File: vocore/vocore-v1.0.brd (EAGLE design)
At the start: 25.6 x 25.6 mm, 146 parts, among them CON2 5020, U1 TFBGA196, U25 U4, U3 SO8, U33 Y1, U35 TSOP2-54P-400MIL, U8 LDO1, U9 LDO1

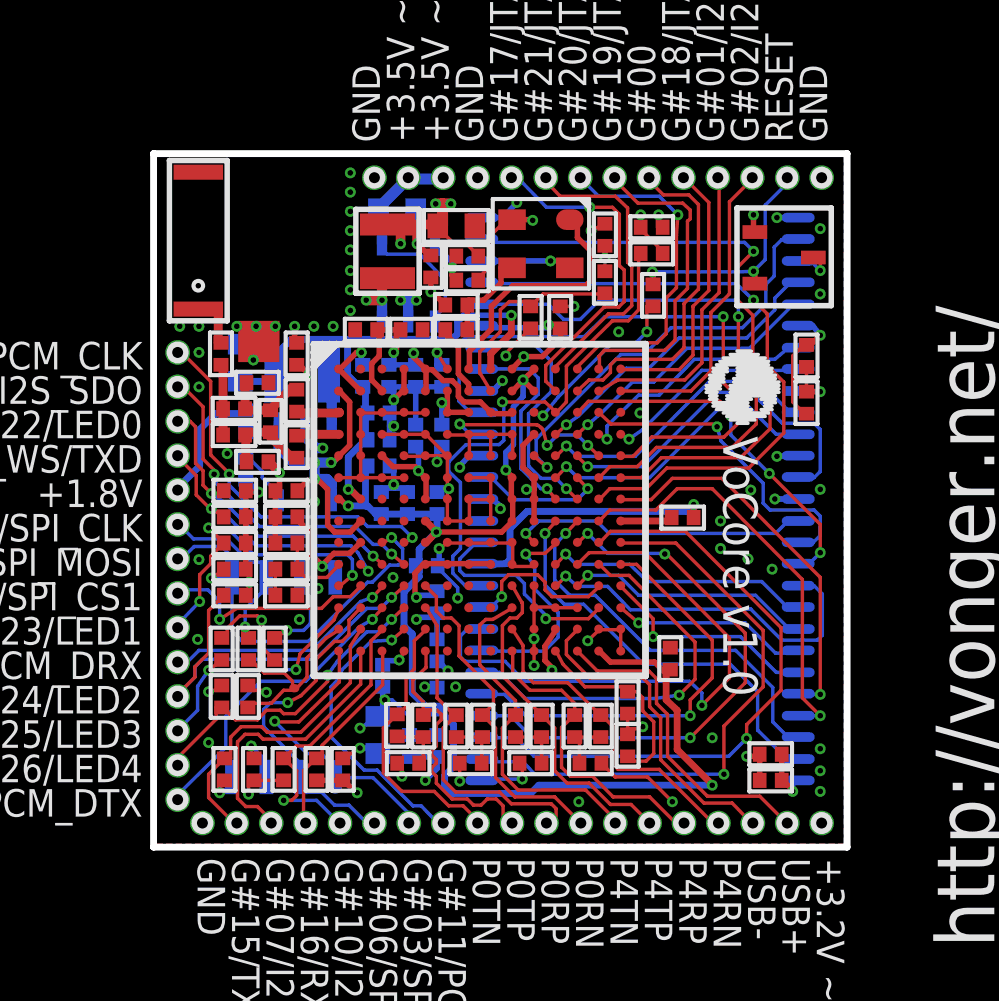
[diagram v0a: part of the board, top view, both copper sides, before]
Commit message: added 4 layer rules.
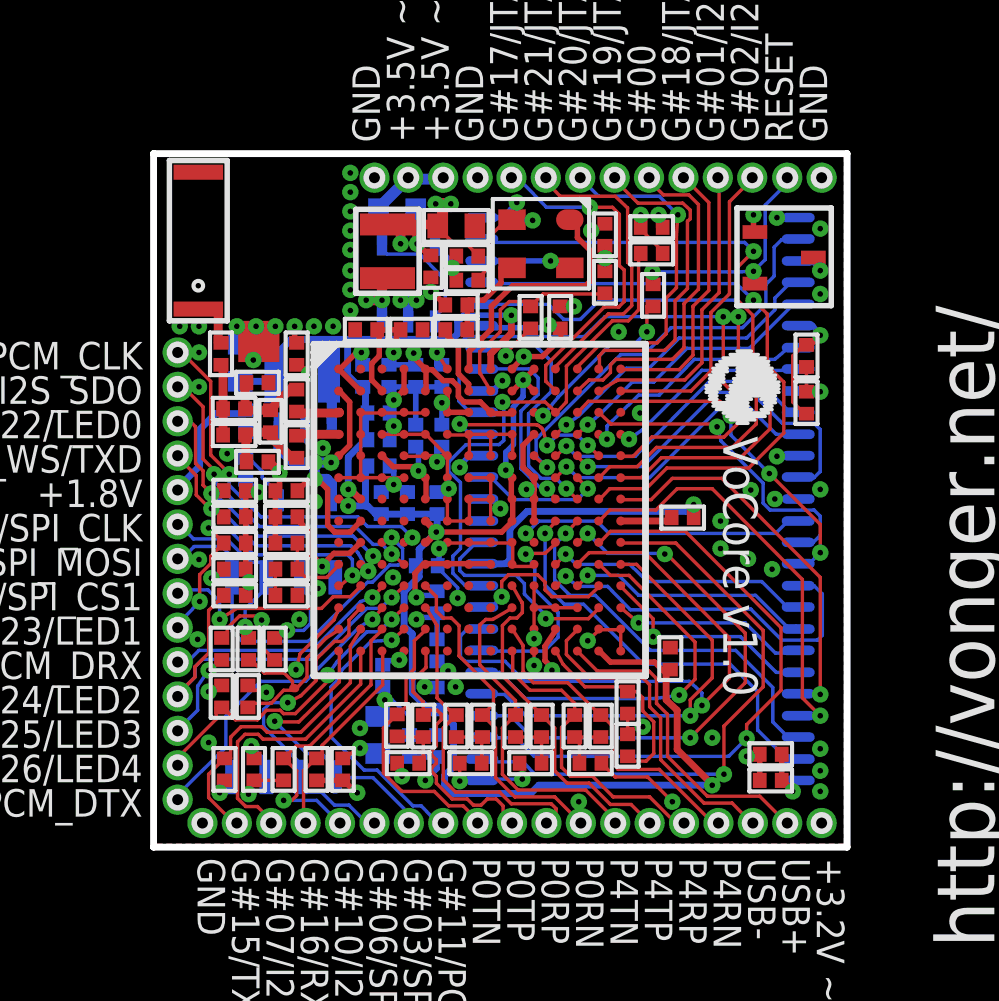
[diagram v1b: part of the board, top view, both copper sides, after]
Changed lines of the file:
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@@
 </class>
 </classes>
-<designrules name="VoCore.v1.0">
-<description language="de">&lt;b&gt;EAGLE Design Rules&lt;/b&gt;
-&lt;p&gt;
-Die Standard-Design-Rules sind so gewählt, dass sie für
-die meisten Anwendungen passen. Sollte ihre Platine
-besondere Anforderungen haben, treffen Sie die erforderlichen
-Einstellungen hier und speichern die Design Rules unter
-einem neuen Namen ab.</description>
+<designrules name="SilverCircuits4layer">
 <description language="en">&lt;b&gt;EAGLE Design Rules&lt;/b&gt;
 &lt;p&gt;
@@
 necessary adjustments and save your customized
 design rules under a new name.</description>
-<param name="layerSetup" value="(1*16)"/>
-<param name="mtCopper" value="0.035mm 0.035mm 0.035mm 0.035mm 0.035mm 0.035mm 0.035mm 0.035mm 0.035mm 0.035mm 0.035mm 0.035mm 0.035mm 0.035mm 0.035mm 0.035mm"/>
-<param name="mtIsolate" value="1.5mm 0.15mm 0.2mm 0.15mm 0.2mm 0.15mm 0.2mm 0.15mm 0.2mm 0.15mm 0.2mm 0.15mm 0.2mm 0.15mm 0.2mm"/>
-<param name="mdWireWire" value="8mil"/>
-<param name="mdWirePad" value="8mil"/>
-<param name="mdWireVia" value="8mil"/>
-<param name="mdPadPad" value="8mil"/>
-<param name="mdPadVia" value="8mil"/>
-<param name="mdViaVia" value="8mil"/>
-<param name="mdSmdPad" value="8mil"/>
-<param name="mdSmdVia" value="8mil"/>
-<param name="mdSmdSmd" value="8mil"/>
+<param name="layerSetup" value="((1*2)*(3*16))"/>
+<param name="mtCopper" value="0.0356mm 0.0356mm 0.0356mm 0.0356mm 0.0356mm 0.0356mm 0.0356mm 0.0356mm 0.0356mm 0.0356mm 0.0356mm 0.0356mm 0.0356mm 0.0356mm 0.0356mm 0.0356mm"/>
+<param name="mtIsolate" value="1.5011mm 0.1499mm 0.2007mm 0.1499mm 0.2007mm 0.1499mm 0.2007mm 0.1499mm 0.2007mm 0.1499mm 0.2007mm 0.1499mm 0.2007mm 0.1499mm 0.2007mm"/>
+<param name="mdWireWire" value="7mil"/>
+<param name="mdWirePad" value="7mil"/>
+<param name="mdWireVia" value="7mil"/>
+<param name="mdPadPad" value="7mil"/>
+<param name="mdPadVia" value="7mil"/>
+<param name="mdViaVia" value="7mil"/>
+<param name="mdSmdPad" value="0mil"/>
+<param name="mdSmdVia" value="0mil"/>
+<param name="mdSmdSmd" value="0mil"/>
 <param name="mdViaViaSameLayer" value="8mil"/>
 <param name="mnLayersViaInSmd" value="2"/>
-<param name="mdCopperDimension" value="40mil"/>
+<param name="mdCopperDimension" value="20mil"/>
 <param name="mdDrill" value="8mil"/>
 <param name="mdSmdStop" value="0mil"/>
-<param name="msWidth" value="10mil"/>
-<param name="msDrill" value="24mil"/>
-<param name="msMicroVia" value="9.99mm"/>
+<param name="msWidth" value="7mil"/>
+<param name="msDrill" value="14mil"/>
+<param name="msMicroVia" value="9.9898mm"/>
 <param name="msBlindViaRatio" value="0.5"/>
-<param name="rvPadTop" value="0"/>
-<param name="rvPadInner" value="0"/>
-<param name="rvPadBottom" value="0"/>
-<param name="rvViaOuter" value="0"/>
-<param name="rvViaInner" value="0"/>
-<param name="rvMicroViaOuter" value="0"/>
-<param name="rvMicroViaInner" value="0"/>
-<param name="rlMinPadTop" value="0mil"/>
-<param name="rlMaxPadTop" value="0mil"/>
-<param name="rlMinPadInner" value="0mil"/>
-<param name="rlMaxPadInner" value="0mil"/>
-<param name="rlMinPadBottom" value="0mil"/>
-<param name="rlMaxPadBottom" value="0mil"/>
-<param name="rlMinViaOuter" value="0mil"/>
-<param name="rlMaxViaOuter" value="0mil"/>
-<param name="rlMinViaInner" value="0mil"/>
-<param name="rlMaxViaInner" value="0mil"/>
-<param name="rlMinMicroViaOuter" value="0mil"/>
-<param name="rlMaxMicroViaOuter" value="0mil"/>
-<param name="rlMinMicroViaInner" value="0mil"/>
-<param name="rlMaxMicroViaInner" value="0mil"/>
+<param name="rvPadTop" value="0.25"/>
+<param name="rvPadInner" value="0.25"/>
+<param name="rvPadBottom" value="0.25"/>
+<param name="rvViaOuter" value="0.25"/>
+<param name="rvViaInner" value="0.25"/>
+<param name="rvMicroViaOuter" value="0.25"/>
+<param name="rvMicroViaInner" value="0.25"/>
+<param name="rlMinPadTop" value="10mil"/>
+<param name="rlMaxPadTop" value="20mil"/>
+<param name="rlMinPadInner" value="10mil"/>
+<param name="rlMaxPadInner" value="20mil"/>
+<param name="rlMinPadBottom" value="10mil"/>
+<param name="rlMaxPadBottom" value="20mil"/>
+<param name="rlMinViaOuter" value="8mil"/>
+<param name="rlMaxViaOuter" value="20mil"/>
+<param name="rlMinViaInner" value="8mil"/>
+<param name="rlMaxViaInner" value="20mil"/>
+<param name="rlMinMicroViaOuter" value="4mil"/>
+<param name="rlMaxMicroViaOuter" value="20mil"/>
+<param name="rlMinMicroViaInner" value="4mil"/>
+<param name="rlMaxMicroViaInner" value="20mil"/>
 <param name="psTop" value="-1"/>
 <param name="psBottom" value="-1"/>
@@
 <param name="checkGrid" value="0"/>
 <param name="checkAngle" value="0"/>
-<param name="checkFont" value="1"/>
+<param name="checkFont" value="0"/>
 <param name="checkRestrict" value="1"/>
 <param name="useDiameter" value="13"/>
@@
 <vertex x="253.0856" y="253.22021875"/>
 </polygon>
-<wire x1="276.7838" y1="276.352" x2="277.3426" y2="274.8788" width="0" layer="19" extent="1-16"/>
+<wire x1="266.2428" y1="270.7386" x2="266.2174" y2="270.764" width="0" layer="19" extent="1-1"/>
 <wire x1="259.8166" y1="269.9512" x2="259.842" y2="269.9512" width="0" layer="19" extent="1-1"/>
 <wire x1="276.7838" y1="255.5748" x2="276.7838" y2="255.5494" width="0" layer="19" extent="16-16"/>
@@
 <wire x1="263.017" y1="263.5504" x2="263.0424" y2="263.5504" width="0" layer="19" extent="1-1"/>
 <wire x1="257.6068" y1="268.7574" x2="257.6068" y2="268.7828" width="0" layer="19" extent="16-16"/>
-<wire x1="266.2174" y1="270.764" x2="266.2428" y2="270.7386" width="0" layer="19" extent="1-1"/>
 <wire x1="267.8176" y1="261.1628" x2="267.843" y2="261.1374" width="0" layer="19" extent="1-1"/>
 <wire x1="263.017" y1="265.9634" x2="263.0424" y2="265.938" width="0" layer="19" extent="1-1"/>
@@
 <wire x1="261.4168" y1="267.5636" x2="261.4422" y2="267.5382" width="0" layer="19" extent="1-1"/>
 <wire x1="267.0302" y1="265.9634" x2="267.0302" y2="266.319" width="0" layer="19" extent="1-1"/>
-<wire x1="277.6474" y1="254" x2="276.5806" y2="255.1684" width="0" layer="19" extent="1-1"/>
-<wire x1="277.0886" y1="270.8402" x2="277.5966" y2="274.3962" width="0" layer="19" extent="1-1"/>
 </signal>
 <signal name="3V3_FB">
@@
 <vertex x="253.0856" y="253.22021875"/>
 </polygon>
-<wire x1="277.5966" y1="275.9456" x2="277.6474" y2="277.8252" width="0" layer="19" extent="1-1"/>
-<wire x1="277.5966" y1="273.5326" x2="277.5966" y2="275.9456" width="0" layer="19" extent="1-1"/>
-<wire x1="277.3172" y1="272.3642" x2="277.5966" y2="273.5326" width="0" layer="19" extent="16-16"/>
-<wire x1="260.2484" y1="278.003" x2="260.2484" y2="277.2918" width="0" layer="19" extent="1-1"/>
-<wire x1="253.9492" y1="272.3388" x2="254.6604" y2="272.3388" width="0" layer="19" extent="1-1"/>
-<wire x1="277.5966" y1="266.319" x2="276.7838" y2="267.5636" width="0" layer="19" extent="16-16"/>
-<wire x1="277.5966" y1="256.7432" x2="275.3614" y2="256.54" width="0" layer="19" extent="1-1"/>
-<wire x1="277.5966" y1="255.9304" x2="277.5966" y2="256.7432" width="0" layer="19" extent="1-1"/>
-<wire x1="277.5966" y1="255.1684" x2="277.5966" y2="255.9304" width="0" layer="19" extent="1-1"/>
 </signal>
 <signal name="JTAG_CLK">

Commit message: fixed air wires.
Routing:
- net SDRAM_CS: track 9.92 -> 12.2 mm
- net +3.3V: track 66.9 -> 68.5 mm
- net +1.2V: track 46.6 -> 47.6 mm
- net SDRAM_DQMU: track 7.85 -> 8.36 mm
